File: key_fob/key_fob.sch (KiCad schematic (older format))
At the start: 20 parts, among them IC1 L4931ABDT33-TR, J1 Arduino-NANO-33, J2 B2B-PH-K-S_LF__SN_, U1 PS1240P02BT

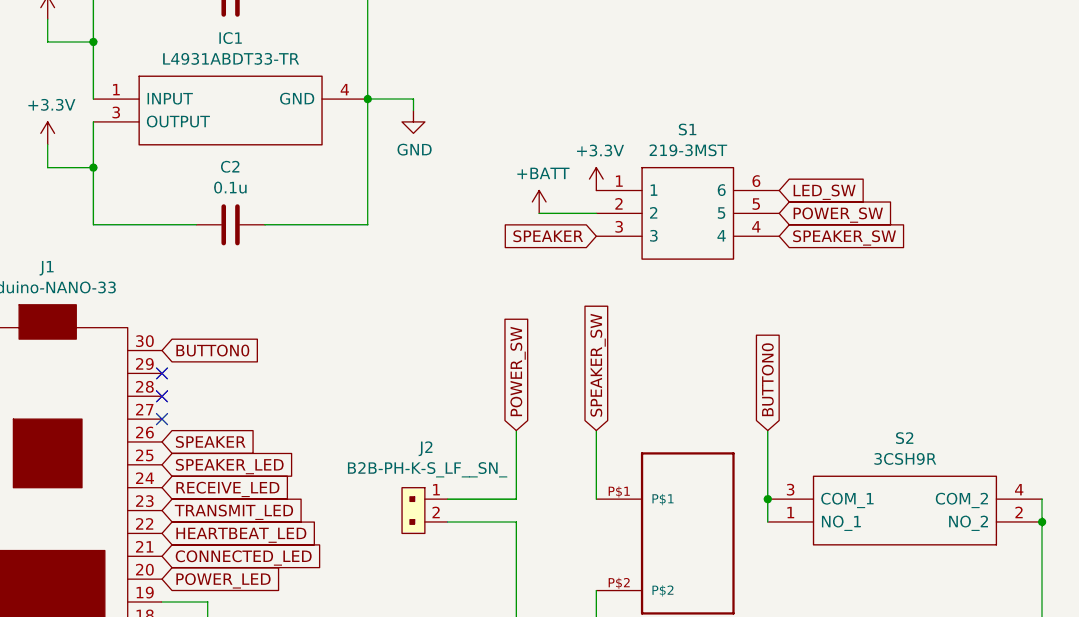
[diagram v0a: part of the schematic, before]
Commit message: First try at placing parts on PCB (no routing)
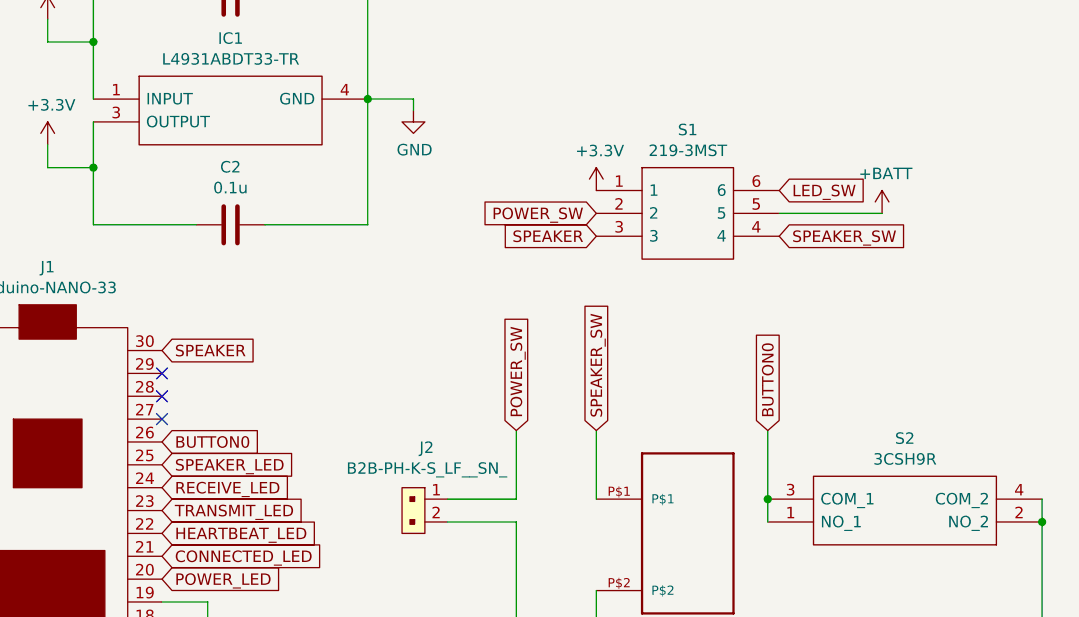
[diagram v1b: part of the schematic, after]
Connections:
- net +BATT: now also S1.5; no longer S1.2
- net BUTTON0: now also J1.26; no longer J1.30
- net POWER_SW: now also S1.2; no longer S1.5
- net SPEAKER: now also J1.30; no longer J1.26
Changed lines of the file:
@@
 Text GLabel 4750 3850 3    50   Input ~ 0
 SPEAKER_LED
-Text GLabel 6350 3300 2    50   Input ~ 0
+Text GLabel 6350 2900 2    50   Input ~ 0
 SPEAKER
 Wire Wire Line
@@
 Wire Wire Line
 	6550 4000 6550 4100
-Text GLabel 6350 2900 2    50   Input ~ 0
+Text GLabel 6350 3300 2    50   Input ~ 0
 BUTTON0
 Text GLabel 6350 3900 2    50   Input ~ 0
@@
 Text GLabel 9050 2200 2    50   Input ~ 0
 LED_SW
-Text GLabel 9050 2300 2    50   Input ~ 0
-POWER_SW
 Text GLabel 9050 2400 2    50   Input ~ 0
 SPEAKER_SW
@@
 	1    0    0    -1
 $EndComp
-Wire Wire Line
-	8250 2300 8000 2300
 $Comp
 L power:+3.3V #PWR0103
@@
 $EndComp
 $Comp
-L power:+BATT #PWR?
+L power:+BATT #PWR0101
 U 1 1 5E5C3234
-P 8000 2300
-F 0 "#PWR?" H 8000 2150 50  0001 C CNN
-F 1 "+BATT" H 8015 2473 50  0000 C CNN
-F 2 "" H 8000 2300 50  0001 C CNN
-F 3 "" H 8000 2300 50  0001 C CNN
-	1    8000 2300
-	1    0    0    -1
-$EndComp
+P 9500 2300
+F 0 "#PWR0101" H 9500 2150 50  0001 C CNN
+F 1 "+BATT" H 9515 2473 50  0000 C CNN
+F 2 "" H 9500 2300 50  0001 C CNN
+F 3 "" H 9500 2300 50  0001 C CNN
+	1    9500 2300
+	1    0    0    -1
+$EndComp
+Text GLabel 8250 2300 0    50   Input ~ 0
+POWER_SW
+Wire Wire Line
+	9500 2300 9050 2300
 $EndSCHEMATC
